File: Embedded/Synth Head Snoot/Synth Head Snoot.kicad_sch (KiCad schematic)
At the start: 19 parts, among them J1 JST [A], J2 10171746-00021LF, J3 JST [K], J4 MSD-1-A, U2 SRV05-4, U4 MAX98357AETE_T

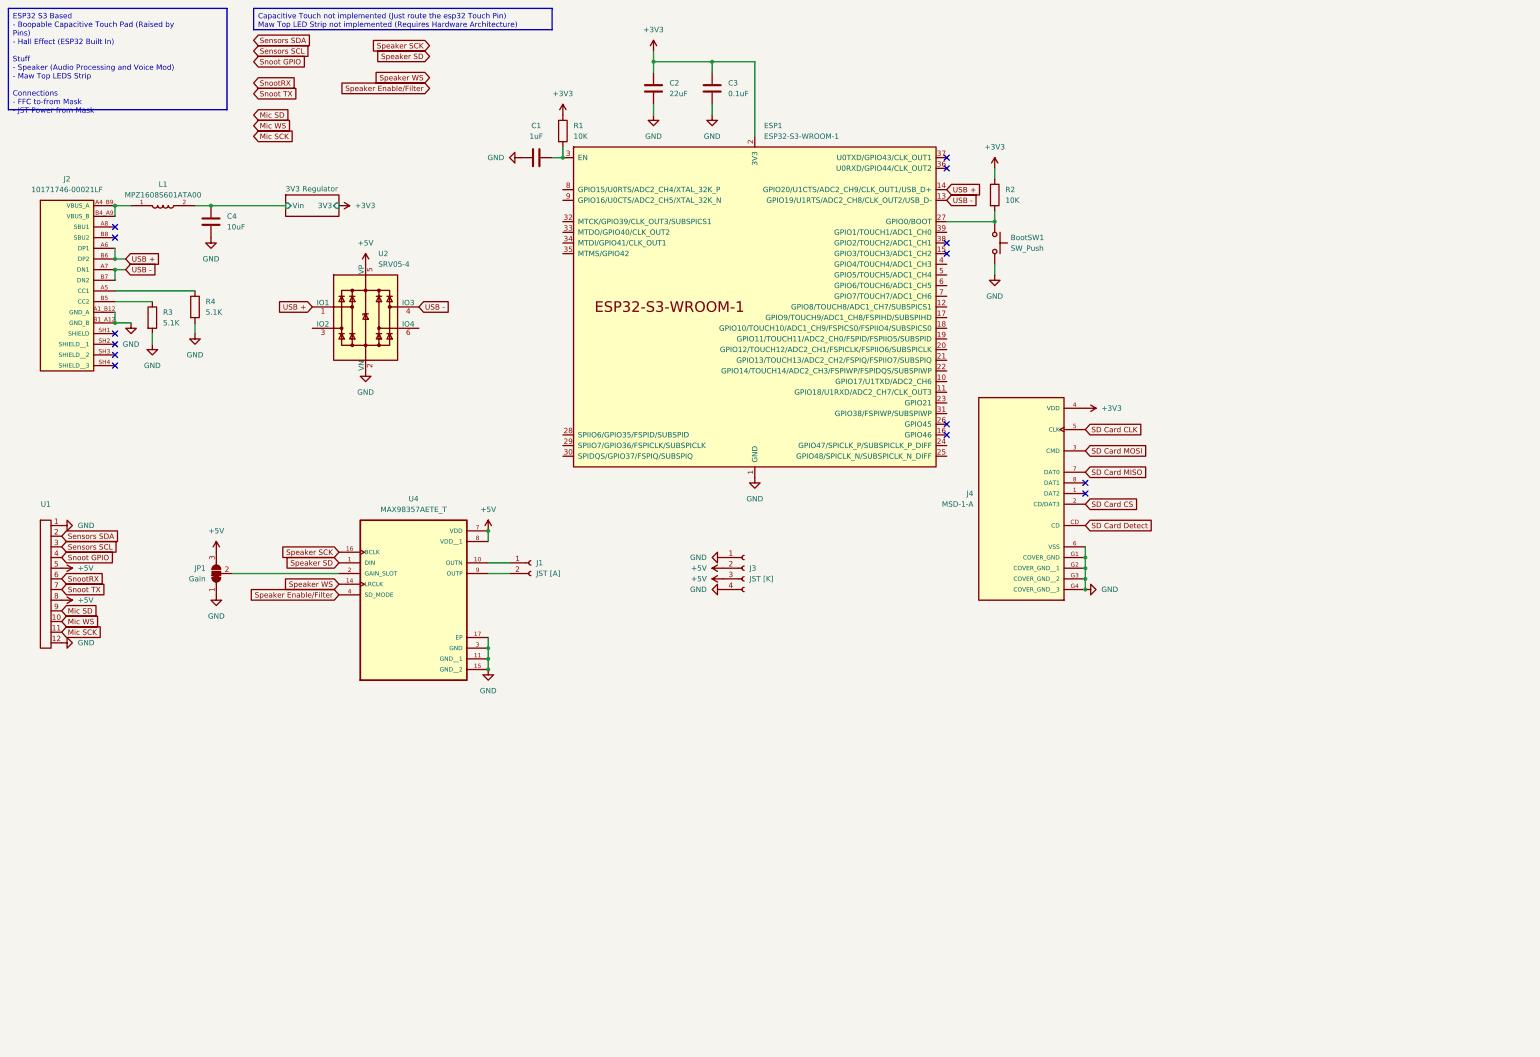
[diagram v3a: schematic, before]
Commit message: Added Touch Pad to Snoot
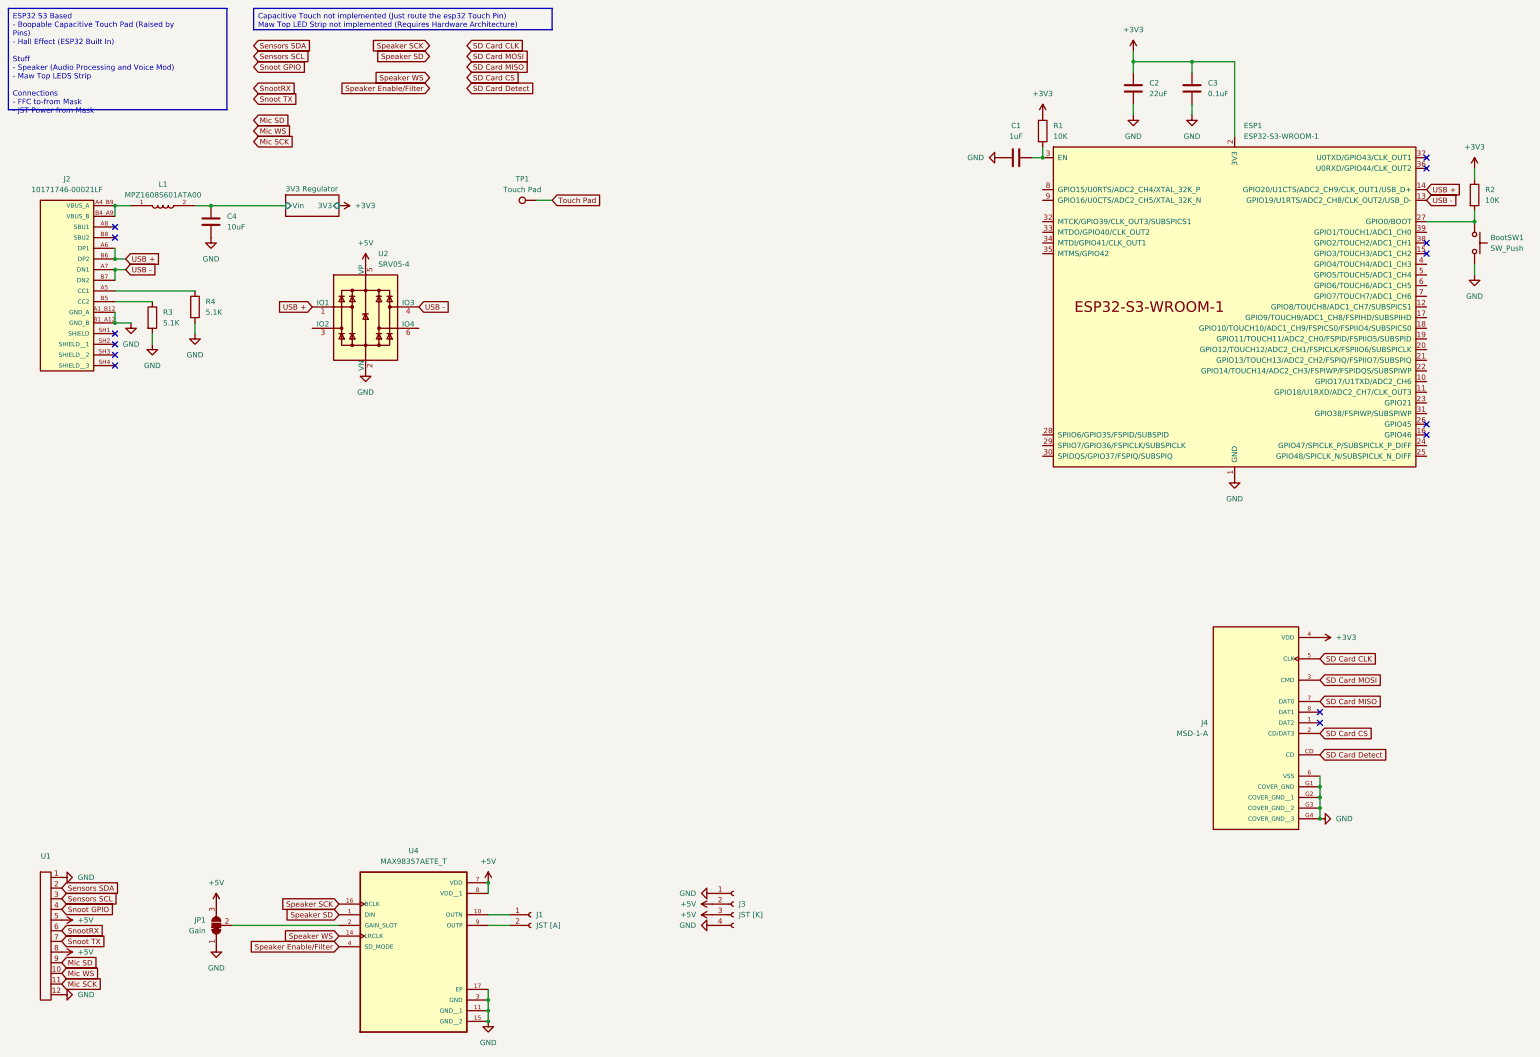
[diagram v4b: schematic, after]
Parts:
- added TP1: Touch Pad, symbol Connector:TestPoint
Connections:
- new net Touch Pad: TP1.1
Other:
- moved on the sheet: BootSW1, C1, C2, C3, ESP1, J1, J3, J4, JP1, R1, R2, U1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

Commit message: Prepared All Main Boards for PCB Creation
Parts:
- added J5, J6: Touch Pad, Connector_PinHeader_2.54mm:PinHeader_1x01_P2.54mm_Vertical, symbol Connector:Conn_01x01_Pin
- added TP2: Touch Pad, TestPoint:TestPoint_Pad_D2.0mm, symbol Connector:TestPoint
- J1: footprint (none) -> Connector_Molex:Molex_PicoBlade_53048-0210_1x02_P1.25mm_Horizontal
- J3: footprint (none) -> Connector_Molex:Molex_PicoBlade_53048-0410_1x04_P1.25mm_Horizontal
- J4: footprint MSD-1-A:CUI_MSD-1-A -> MicroSD_MSD_1_A:CUI_MSD-1-A
- JP1: footprint (none) -> Jumper:SolderJumper-3_P1.3mm_Bridged12_Pad1.0x1.5mm_NumberLabels
- TP1: footprint (none) -> TestPoint:TestPoint_Pad_D2.0mm
- U1: value ~ -> FFC [S]; footprint (none) -> FFC_Connector:FFC Aliexpress 0.5mm 12P
- U4: footprint MAX98357AETE_T:QFN50P300X300X80-17N -> I2S_Audio_MAX98357A:QFN50P300X300X80-17N
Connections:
- net Touch Pad: now also J5.1 (Pin_1)
- new net: J6.1 (Pin_1), TP2.1

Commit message: Prepared Circuits for Routing and Placement Tuning
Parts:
- C3: footprint Capacitor_SMD:C_0603_1608Metric -> Capacitor_SMD:C_0603_1608Metric_Pad1.08x0.95mm_HandSolder
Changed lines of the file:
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@@
 			)
 		)
-		(property "Footprint" "Capacitor_SMD:C_0603_1608Metric"
+		(property "Footprint" "Capacitor_SMD:C_0603_1608Metric_Pad1.08x0.95mm_HandSolder"
 			(at 300.6852 40.64 0)
 			(effects
